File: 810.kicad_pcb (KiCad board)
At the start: 2 copper layers, 148 x 110.1 mm, 294 parts, among them J1 PJ301BM, J10 PJ301BM, J11 PJ301BM, J12 PJ301BM, J13 PJ301BM, J14 PJ301BM, J15 JACK_MONO_SW, J16 PJ301BM, J17 PJ301B, J18 PJ301B, J2 PJ301BM, J3 PJ301BM, J4 PJ301B, J5 PJ301B, J6 PJ301BM, J7 PJ301BM, J8 PJ301BM, J9 PJ301BM, P1 CONN_01X08, P2 CONN_02X05, P3 CONN_01X03, P4 CONN_01X08, Q1 PMBT2369, Q10 2SK208-GR, Q11 2SC4738, Q12 2SA1832, Q13 2SA1832, Q14 2SA1832, Q2 2SK208-GR, Q3 2SA1618, Q4 2SC4207, Q5 2SK208-GR, Q6 MMBF4391LT1G, Q7 2SA1832, Q8 PMBT2369, Q9 2SK208-GR, SW1 SPDT, SW2 SPDT, SW3 BF3-1050, SW4 SPDT, SW5 DP6T-ALPHA-SR2511, U1 TL072-, U10 RC4558, U11 TL074-, U12 TA75S558F, U13 TA75S558F, U14 TA75S558F, U15 TA75S558F, U16 TA75S558F, U17 CD4052, U18 TA75S558F, U2 TL072-, U3 TL072-, U4 CD40106, U5 CD4027, U6 LM13700, U7 LM13700, U8 LM13700, U9 TL072-

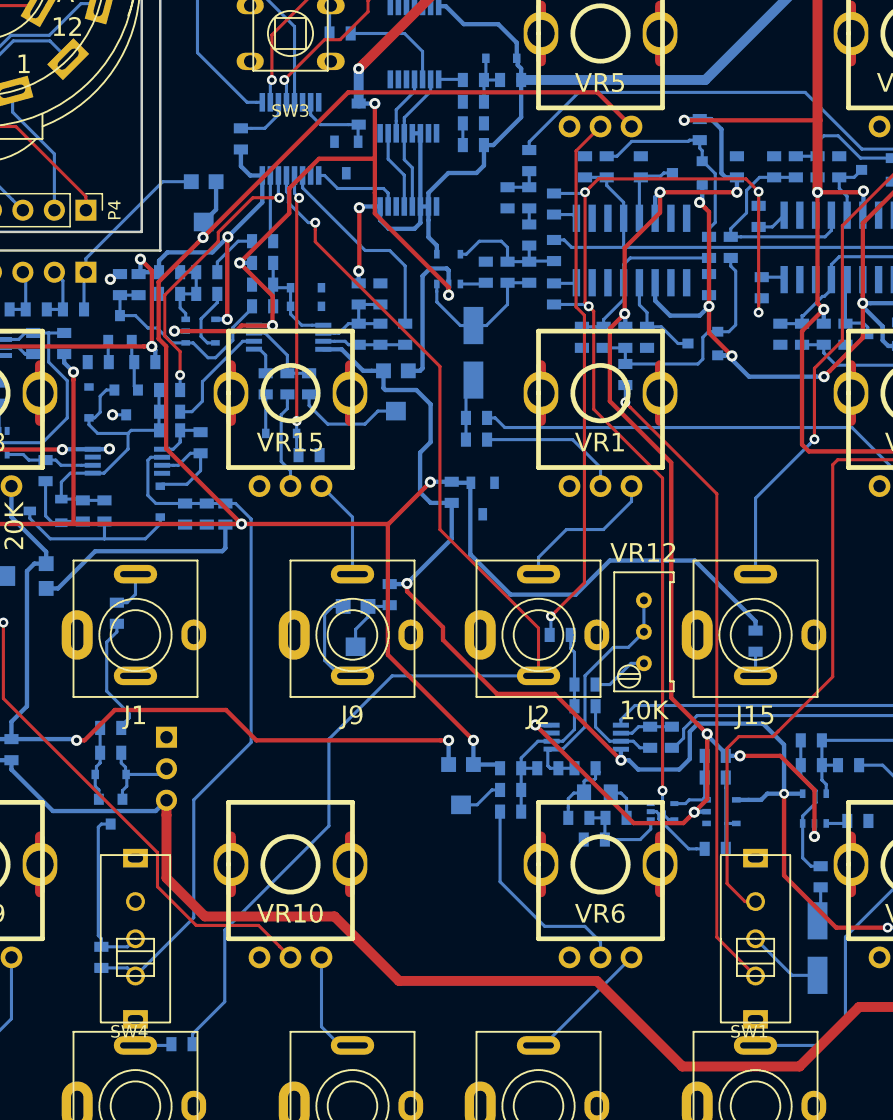
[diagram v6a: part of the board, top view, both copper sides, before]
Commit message: main power rails routed
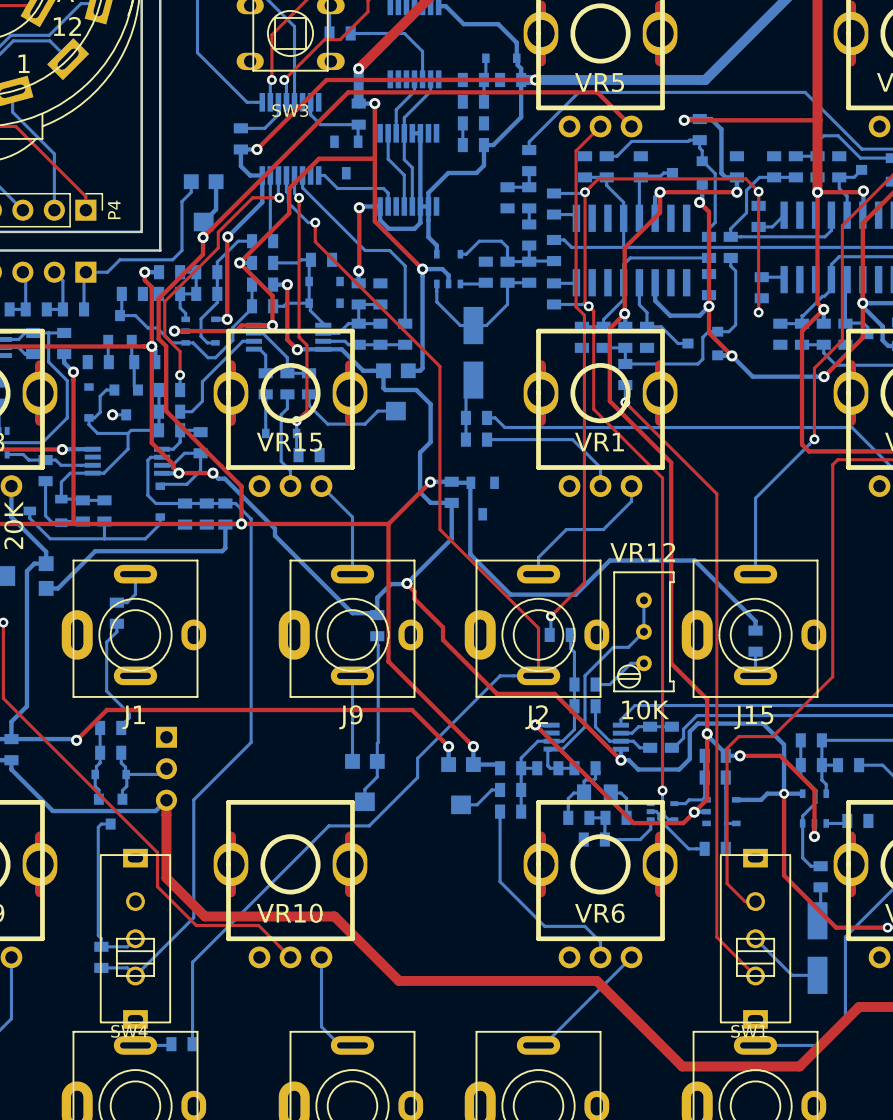
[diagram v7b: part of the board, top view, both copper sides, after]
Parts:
- moved VR14 12.5 mm to (126.5, 119.5)
- moved R66 10.0 mm to (118.2, 79.2), turned to 0 degrees
- moved R82 5.15 mm to (123.0, 77.2), turned to 180 degrees
- moved R55 2.69 mm to (127.5, 106.8)
- moved D9 1.58 mm to (123.2, 79.0)
- moved D8 1.52 mm to (123.2, 80.8)
- moved R68 1.25 mm to (107.8, 80.0), turned to 180 degrees
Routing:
- net +12V: track 609.8 -> 670.4 mm, vias 23 -> 29
- net Net-(R55-Pad1): track 5.46 -> 14.0 mm
- net -12V: track 758.6 -> 753.4 mm, vias 31 -> 30
- net VCO: track 97.3 -> 94.1 mm
- net Net-(P1-Pad1): track 15.2 -> 17.4 mm
- net Net-(D8-Pad1): track 10.1 -> 12.0 mm
- net Net-(C17-Pad2): track 9.67 -> 11.4 mm
- net GND: track 2.08 -> 1.10 mm, vias 2 -> 1
- net VCO_PULSE: track 22.9 -> 23.4 mm

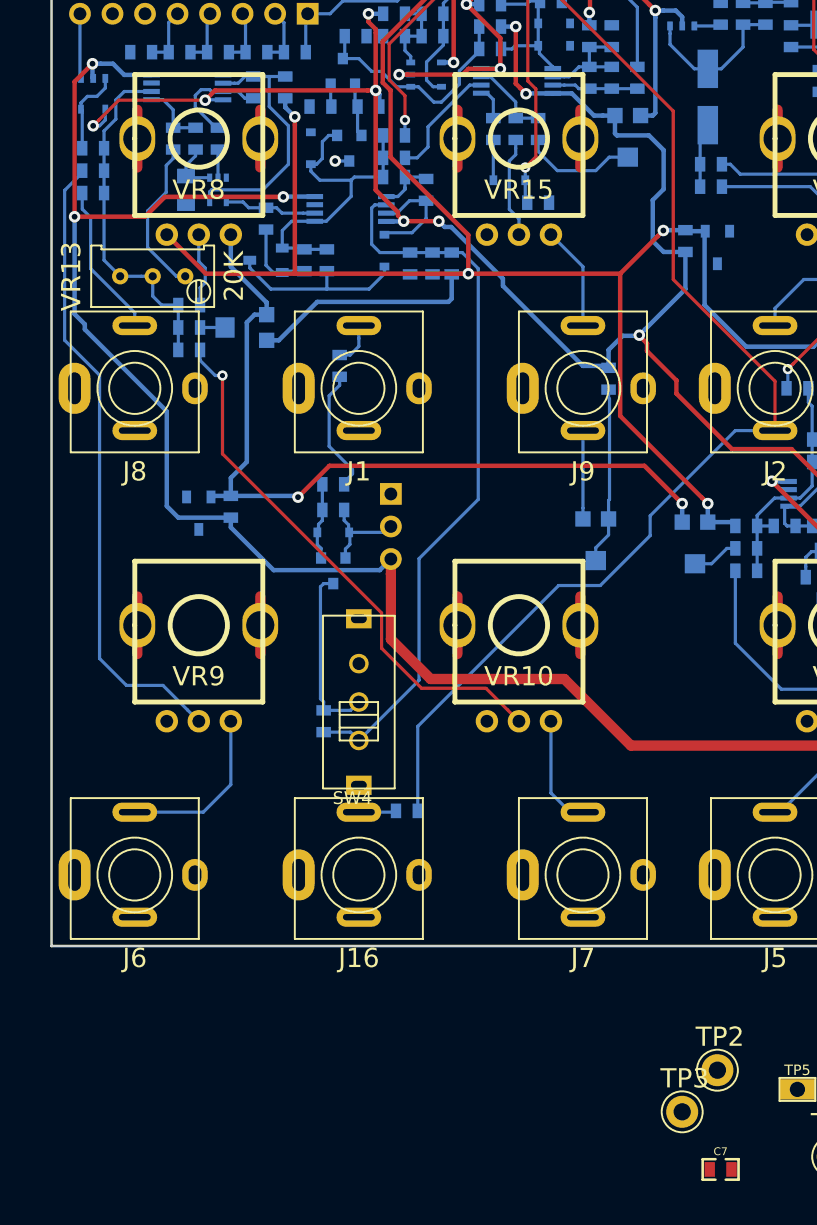
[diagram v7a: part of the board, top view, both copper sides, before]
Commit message: placed and routed previously unplaced C7
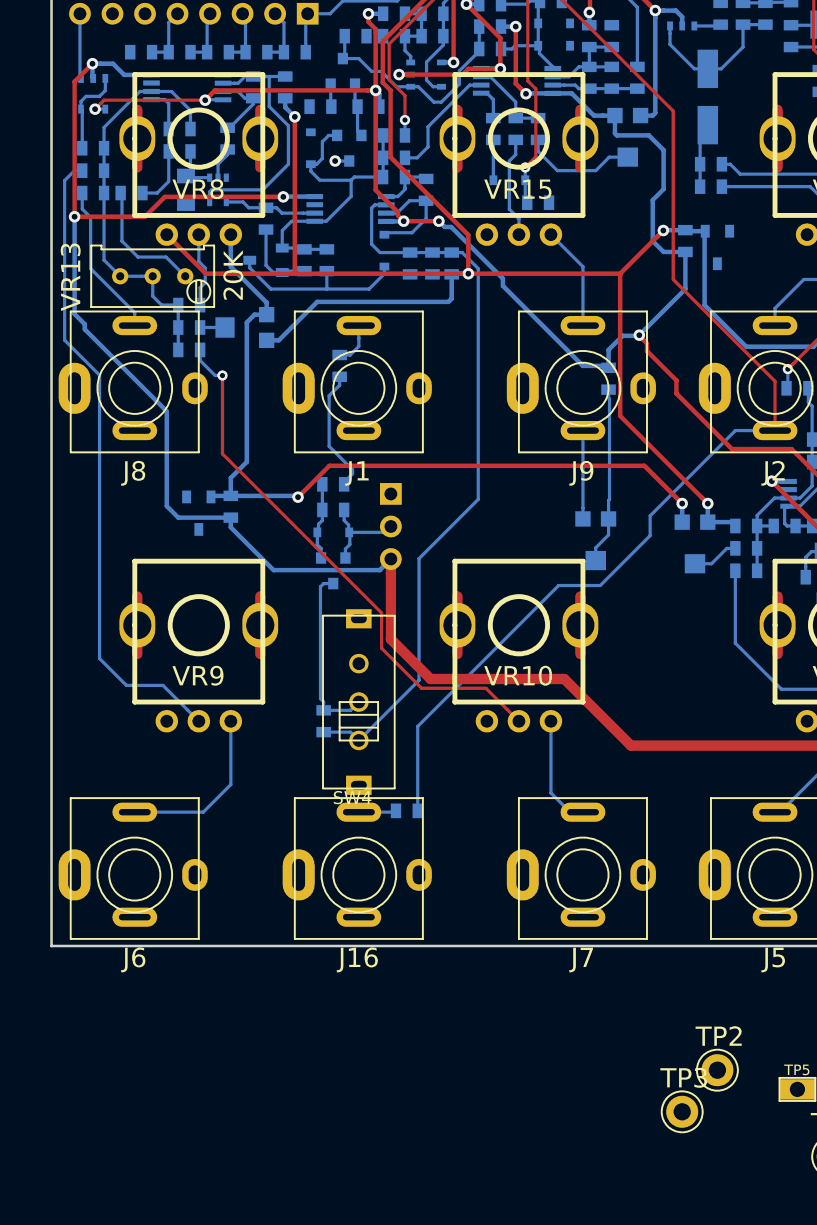
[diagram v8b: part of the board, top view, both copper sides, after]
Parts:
- C7: moved to B.Cu
- moved C7 91.6 mm to (94.0, 87.2)
- moved R37 5.35 mm to (90.2, 92.2), turned to 0 degrees
- moved R47 1.60 mm to (94.0, 89.0), turned to 0 degrees
- moved R51 0.75 mm to (97.8, 88.0)
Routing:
- net Net-(C7-Pad1): track 5.17 -> 9.99 mm
- net Net-(C7-Pad2): track 27.6 -> 32.0 mm
- net Net-(R37-Pad1): track 12.3 -> 9.87 mm
- net Net-(C9-Pad2): track 8.35 -> 5.96 mm
- net +12V: track 670.4 -> 668.5 mm
